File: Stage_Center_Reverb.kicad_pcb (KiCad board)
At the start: 2 copper layers, 75 x 50 mm, 42 parts, among them J10 Power, J2 Output, J3 Tank, U1 TL072, U10 L78L15, U11 L79L15, U2 TL072

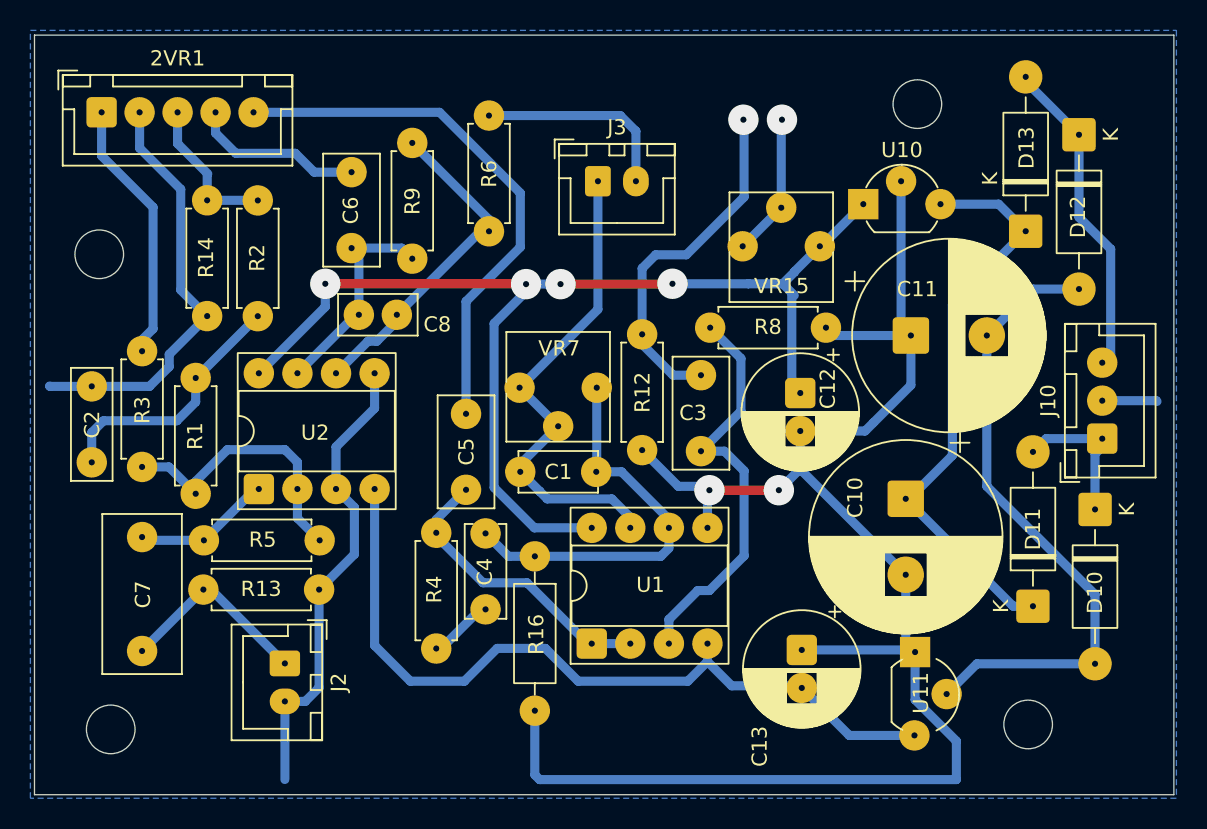
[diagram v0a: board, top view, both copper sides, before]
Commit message: パッドの大きさとドリル穴を2に変更
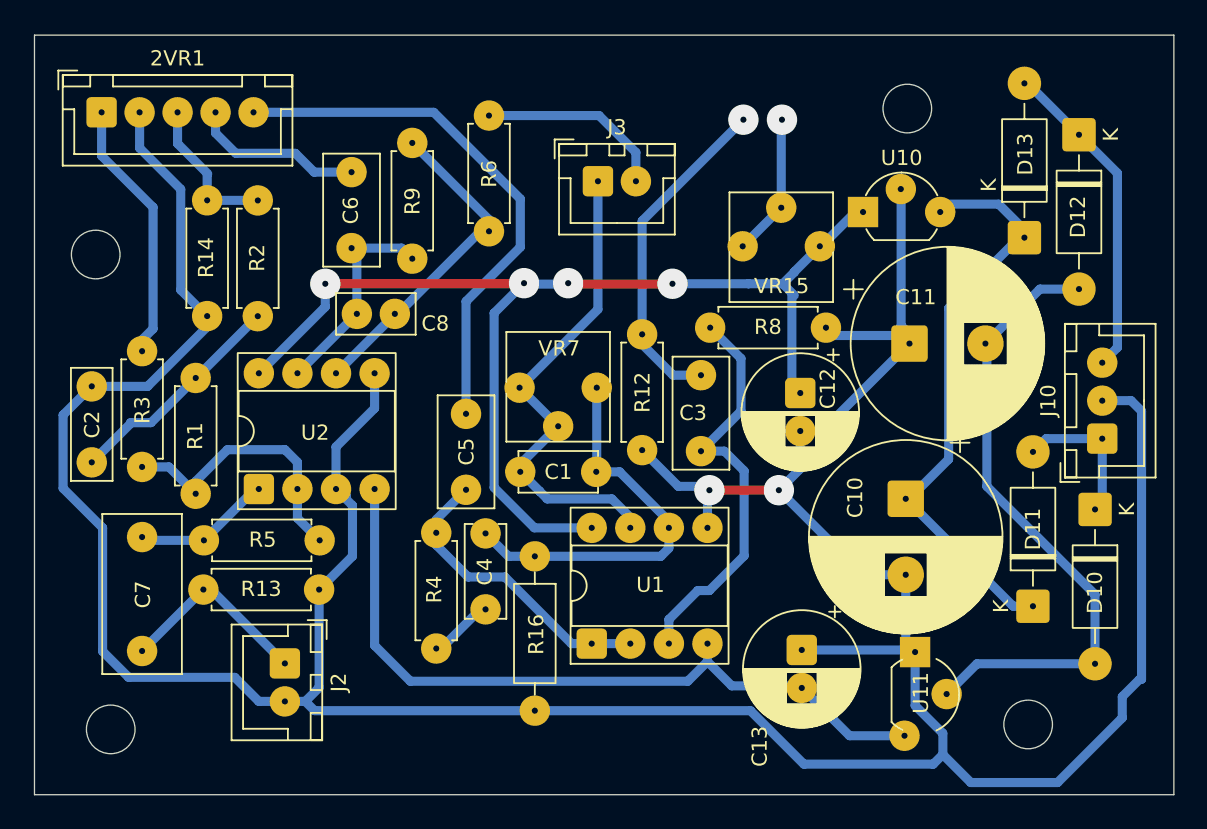
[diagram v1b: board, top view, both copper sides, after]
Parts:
- moved H2 0.72 mm to (151.0, 81.3)
- moved C11 0.54 mm to (151.1, 96.8)
- moved U10 0.52 mm to (148.0, 88.1)
- moved D13 0.43 mm to (158.7, 89.8)
- moved H1 0.23 mm to (97.5, 90.9)
- moved C8 0.14 mm to (117.2, 94.8)
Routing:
- net GNDPWR: track 173.0 -> 241.2 mm
- net -15V: track 52.3 -> 49.8 mm
- net Net-(C2-Pad1): track 17.0 -> 14.9 mm
- net Net-(J3-Pin_2): track 13.4 -> 12.6 mm
- net Net-(C6-Pad1): track 14.7 -> 15.4 mm
- removed copper zone on B.Cu, net GNDPWR

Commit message: 配線を0.6にして修正
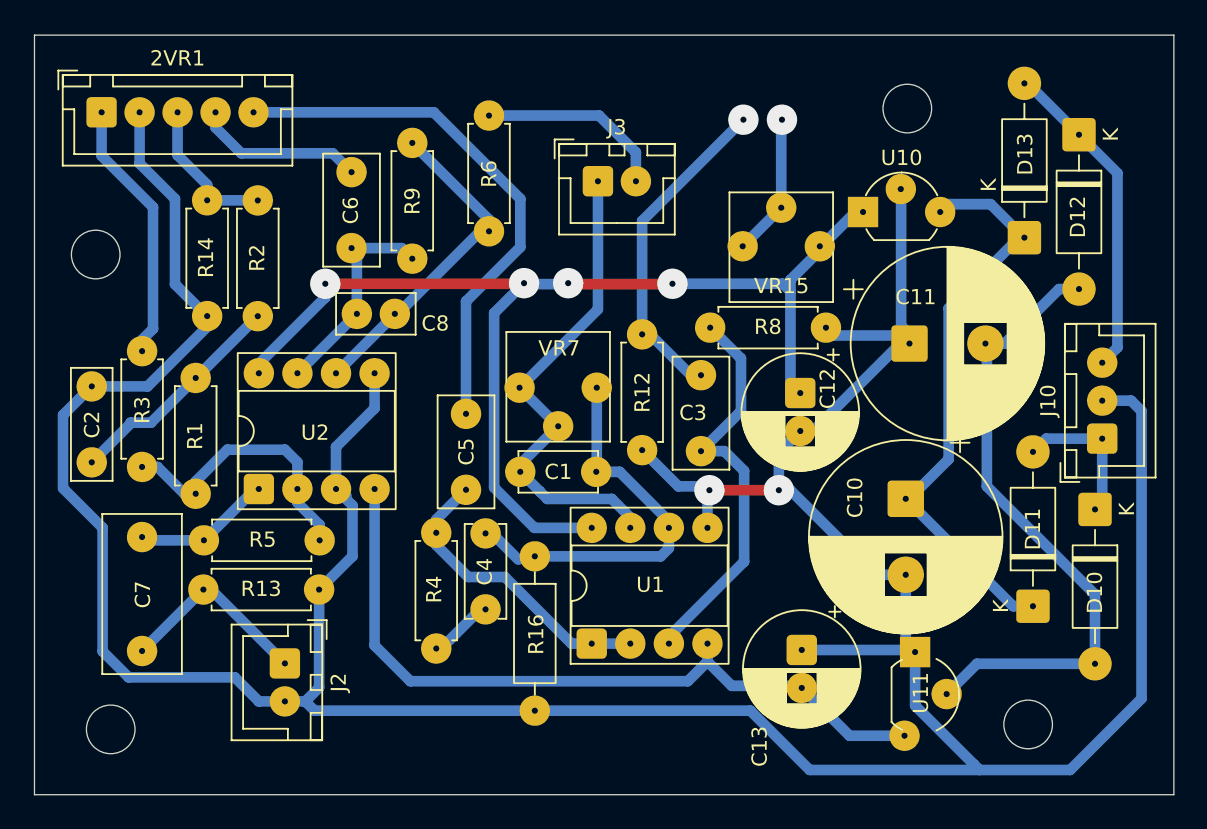
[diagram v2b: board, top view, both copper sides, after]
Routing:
- net Net-(U1B--): track 27.5 -> 26.5 mm
- net +15V: track 74.8 -> 75.6 mm
- net GNDPWR: track 241.2 -> 241.9 mm

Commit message: 配線を修正、幅は0.8に。この回路で一旦完成。
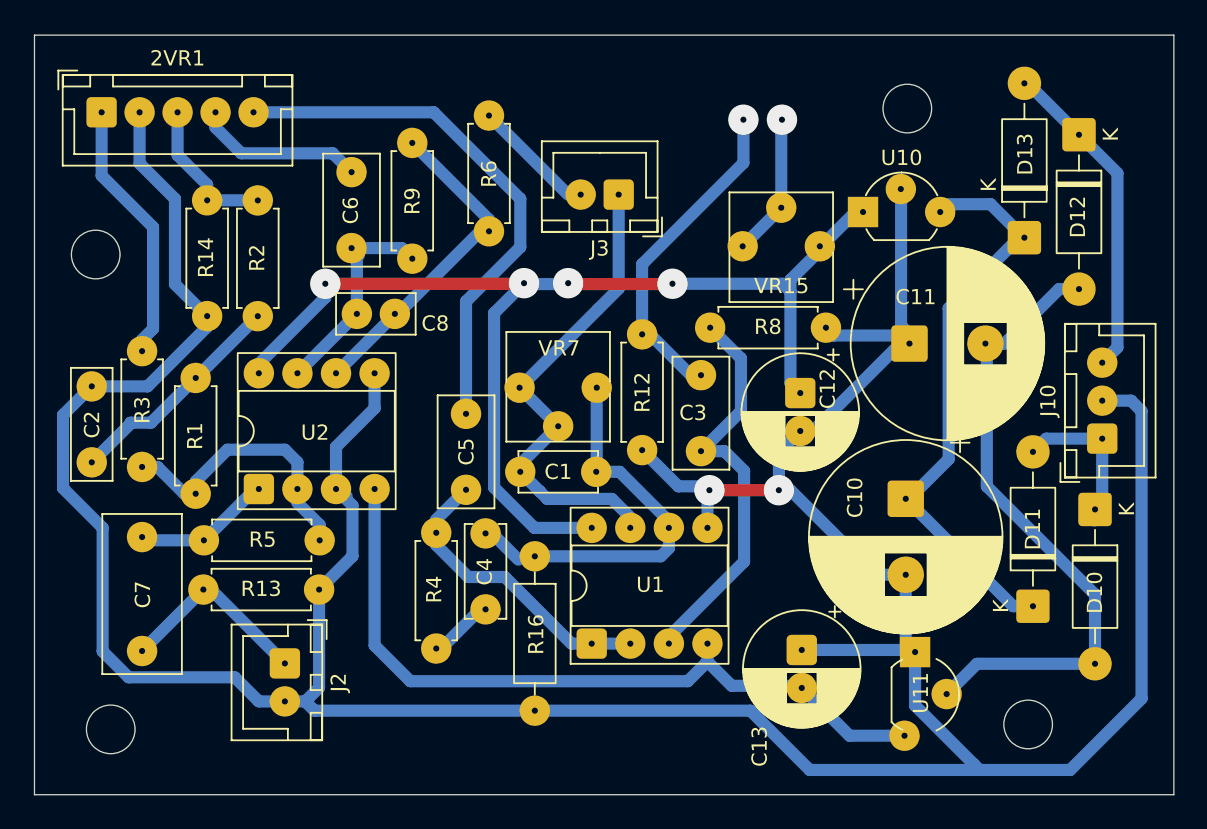
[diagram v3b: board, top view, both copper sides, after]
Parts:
- moved J3 1.62 mm to (132.0, 87.0), turned to 180 degrees
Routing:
- net Net-(J3-Pin_2): track 12.6 -> 8.19 mm
